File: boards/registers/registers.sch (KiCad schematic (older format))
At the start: 51 parts

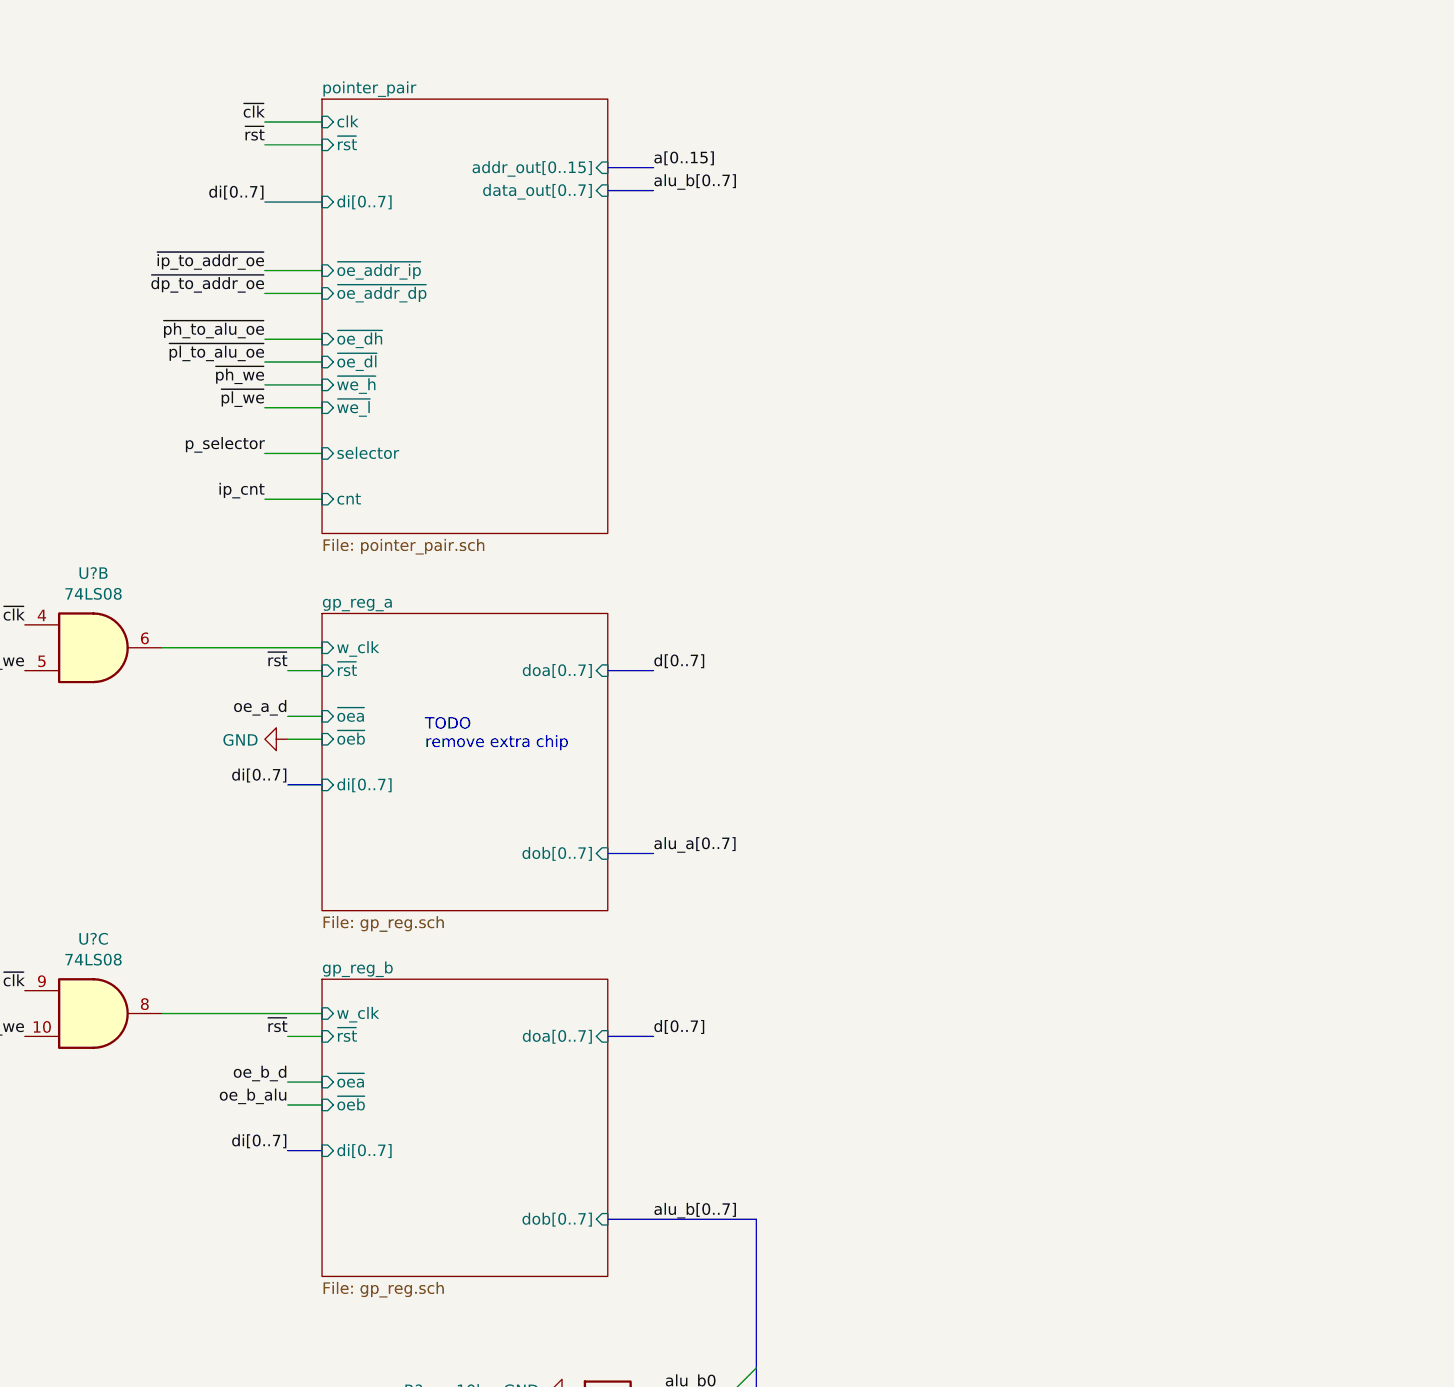
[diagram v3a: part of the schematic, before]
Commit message: Remove redundant chip from the register A, change hierarchical pin types
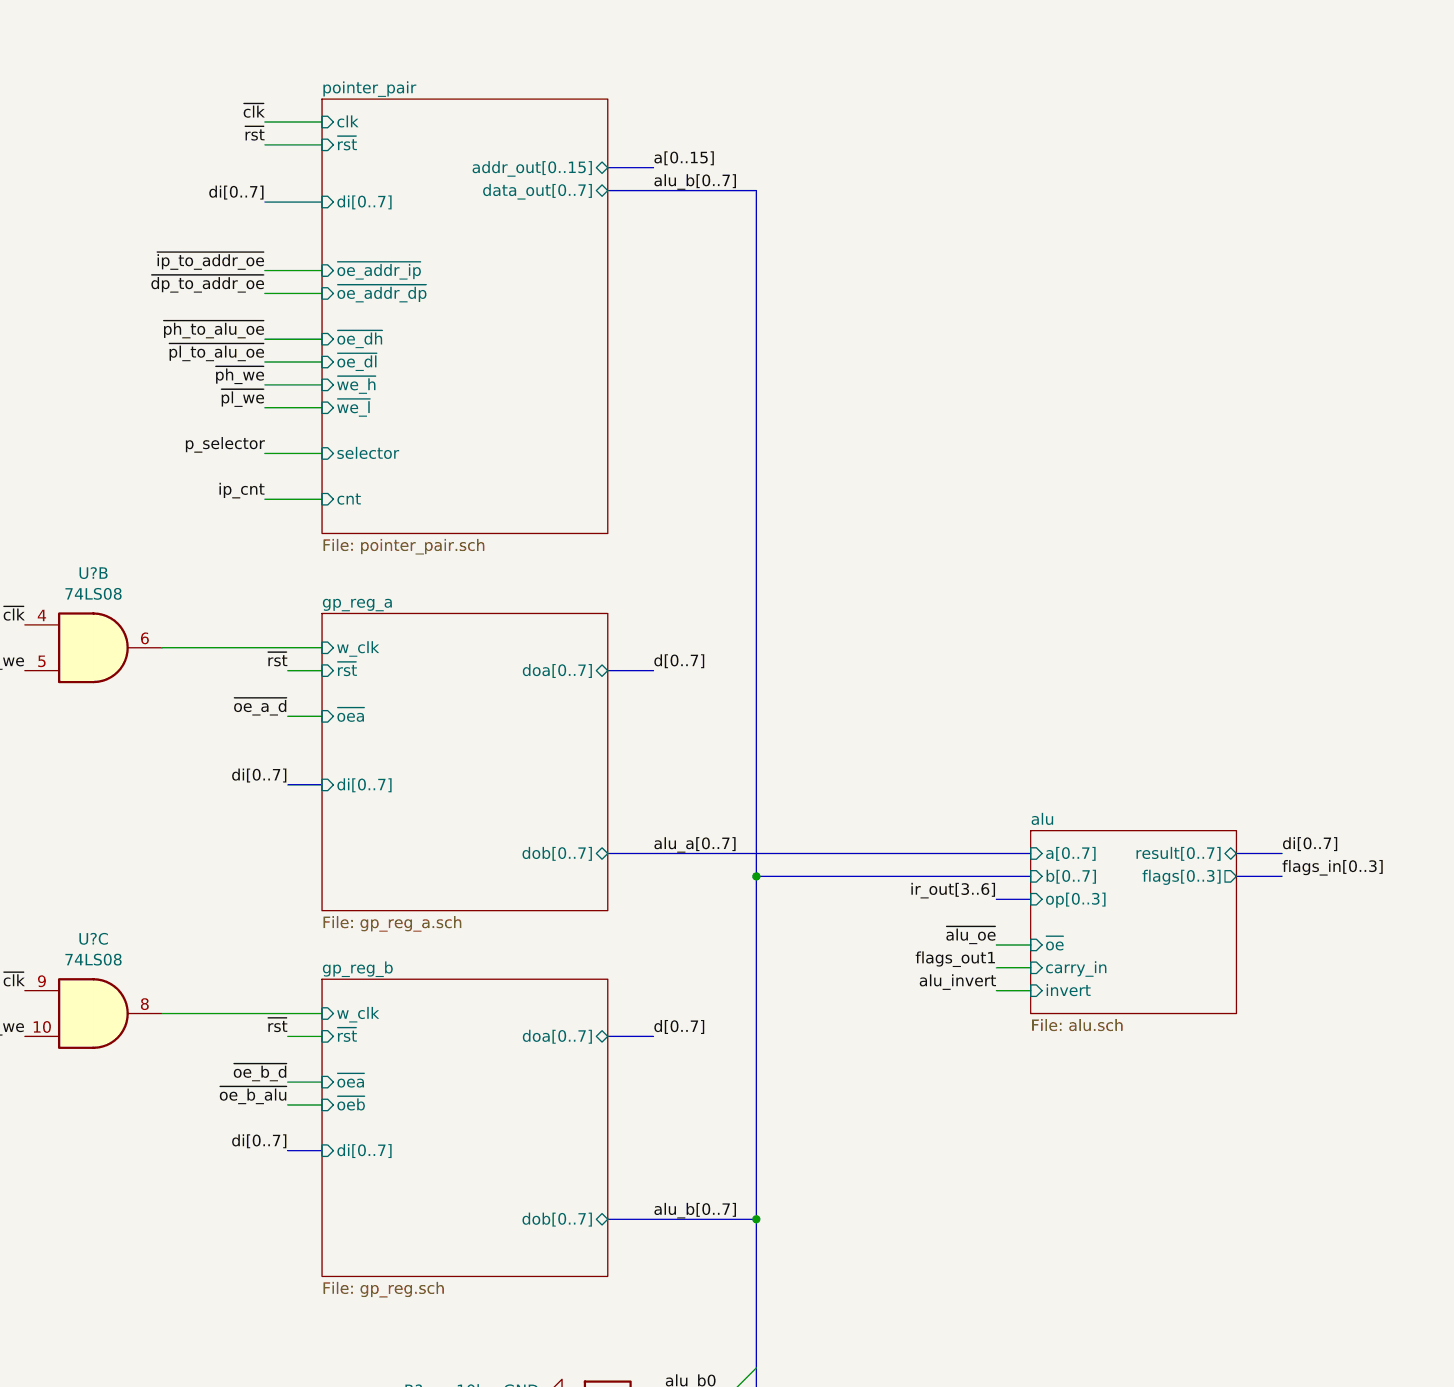
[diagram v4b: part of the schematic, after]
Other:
- note removed: "TODO\nremove extra chip"
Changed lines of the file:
@@
 $Descr A3 16535 11693
 encoding utf-8
-Sheet 1 6
+Sheet 1 7
 Title "CPU registers and memory module"
 Date "2019-12-28"
@@
 F11 "~we_l" I L 10150 2400 50
 F12 "selector" I L 10150 2600 50
-F13 "addr_out[0..15]" I R 11400 1350 50
-F14 "data_out[0..7]" I R 11400 1450 50
+F13 "addr_out[0..15]" T R 11400 1350 50
+F14 "data_out[0..7]" T R 11400 1450 50
 $EndSheet
 Wire Bus Line
@@
 Text Label 9900 1500 2    50   ~ 0
 di[0..7]
-Wire Bus Line
-	11400 1450 11600 1450
 Text Label 11600 1450 0    50   ~ 0
 alu_b[0..7]
@@
 ir_we
 $Sheet
-S 10150 3300 1250 1300
-U 5E73B7F6
-F0 "gp_reg_a" 50
-F1 "gp_reg.sch" 50
-F2 "w_clk" I L 10150 3450 50
-F3 "~rst" I L 10150 3550 50
-F4 "~oea" I L 10150 3750 50
-F5 "~oeb" I L 10150 3850 50
-F6 "di[0..7]" I L 10150 4050 50
-F7 "doa[0..7]" I R 11400 3550 50
-F8 "dob[0..7]" I R 11400 4350 50
-$EndSheet
-$Sheet
 S 10150 4900 1250 1300
 U 5E7CA397
@@
 F5 "~oeb" I L 10150 5450 50
 F6 "di[0..7]" I L 10150 5650 50
-F7 "doa[0..7]" I R 11400 5150 50
-F8 "dob[0..7]" I R 11400 5950 50
+F7 "doa[0..7]" T R 11400 5150 50
+F8 "dob[0..7]" T R 11400 5950 50
 $EndSheet
 $Comp
@@
 Wire Wire Line
 	10150 3750 10000 3750
-Wire Wire Line
-	10150 3850 10000 3850
 Wire Bus Line
 	10150 4050 10000 4050
@@
 di[0..7]
 Text Label 10000 3750 2    50   ~ 0
-oe_a_d
-$Comp
-L power:GND #PWR?
-U 1 1 5E7EB4E9
-P 10000 3850
-F 0 "#PWR?" H 10000 3600 50  0001 C CNN
-F 1 "GND" V 10005 3722 50  0000 R CNN
-F 2 "" H 10000 3850 50  0001 C CNN
-F 3 "" H 10000 3850 50  0001 C CNN
-	1    10000 3850
-	0    1    1    0
-$EndComp
-Text Notes 10600 3900 0    50   ~ 0
-TODO\nremove extra chip
-Wire Bus Line
-	11400 3550 11600 3550
+~oe_a_d
 Text Label 11600 4350 0    50   ~ 0
 alu_a[0..7]
 Text Label 11600 3550 0    50   ~ 0
 d[0..7]
-Wire Bus Line
-	11600 4350 11400 4350
 Wire Bus Line
 	11400 5150 11600 5150
@@
 di[0..7]
 Text Label 10000 5350 2    50   ~ 0
-oe_b_d
+~oe_b_d
 Text Label 10000 5450 2    50   ~ 0
-oe_b_alu
+~oe_b_alu
 Text Label 8850 4950 2    50   ~ 0
 ~clk
@@
 U 1 1 5E9A723F
 P 6000 1100
+AR Path="/5E7CA397/5E9A723F" Ref="R?"  Part="1"
+AR Path="/5E9A723F" Ref="R?"  Part="1"
 F 0 "R?" V 6000 1900 50  0000 C CNN
 F 1 "1k" V 6000 1750 50  0000 C CNN
@@
 U 1 1 5E9A7245
 P 6000 1200
+AR Path="/5E7CA397/5E9A7245" Ref="R?"  Part="1"
+AR Path="/5E9A7245" Ref="R?"  Part="1"
 F 0 "R?" V 6000 2000 50  0000 C CNN
 F 1 "1k" V 6000 1850 50  0000 C CNN
@@
 U 1 1 5E9A724B
 P 6000 1300
+AR Path="/5E7CA397/5E9A724B" Ref="R?"  Part="1"
+AR Path="/5E9A724B" Ref="R?"  Part="1"
 F 0 "R?" V 6000 2100 50  0000 C CNN
 F 1 "1k" V 6000 1950 50  0000 C CNN
@@
 U 1 1 5E9A7251
 P 6000 1400
+AR Path="/5E7CA397/5E9A7251" Ref="R?"  Part="1"
+AR Path="/5E9A7251" Ref="R?"  Part="1"
 F 0 "R?" V 6000 2200 50  0000 C CNN
 F 1 "1k" V 6000 2050 50  0000 C CNN
@@
 U 1 1 5E9A7257
 P 6000 1500
+AR Path="/5E7CA397/5E9A7257" Ref="R?"  Part="1"
+AR Path="/5E9A7257" Ref="R?"  Part="1"
 F 0 "R?" V 6000 2300 50  0000 C CNN
 F 1 "1k" V 6000 2150 50  0000 C CNN
@@
 U 1 1 5E9A725D
 P 6000 1600
+AR Path="/5E7CA397/5E9A725D" Ref="R?"  Part="1"
+AR Path="/5E9A725D" Ref="R?"  Part="1"
 F 0 "R?" V 6000 2400 50  0000 C CNN
 F 1 "1k" V 6000 2250 50  0000 C CNN
@@
 U 1 1 5E9A7263
 P 6000 1700
+AR Path="/5E7CA397/5E9A7263" Ref="R?"  Part="1"
+AR Path="/5E9A7263" Ref="R?"  Part="1"
 F 0 "R?" V 6000 2500 50  0000 C CNN
 F 1 "1k" V 6000 2350 50  0000 C CNN
@@
 U 1 1 5E9A7269
 P 6000 1800
+AR Path="/5E7CA397/5E9A7269" Ref="R?"  Part="1"
+AR Path="/5E9A7269" Ref="R?"  Part="1"
 F 0 "R?" V 6000 2600 50  0000 C CNN
 F 1 "1k" V 6000 2450 50  0000 C CNN
@@
 	0    1    1    0
 $EndComp
+$Sheet
+S 13250 4250 900  800
+U 5E9B4830
+F0 "alu" 50
+F1 "alu.sch" 50
+F2 "a[0..7]" I L 13250 4350 50
+F3 "b[0..7]" I L 13250 4450 50
+F4 "op[0..3]" I L 13250 4550 50
+F5 "~oe" I L 13250 4750 50
+F6 "carry_in" I L 13250 4850 50
+F7 "invert" I L 13250 4950 50
+F8 "result[0..7]" T R 14150 4350 50
+F9 "flags[0..3]" O R 14150 4450 50
+$EndSheet
+Wire Bus Line
+	12050 5950 12050 4450
+Wire Bus Line
+	12050 4450 13250 4450
+Connection ~ 12050 5950
+Wire Bus Line
+	12050 1450 12050 4450
+Wire Bus Line
+	11400 1450 12050 1450
+Connection ~ 12050 4450
+Wire Wire Line
+	13250 4750 13100 4750
+Wire Wire Line
+	13250 4850 13100 4850
+Wire Wire Line
+	13250 4950 13100 4950
+Text Label 13100 4750 2    50   ~ 0
+~alu_oe
+Text Label 13100 4850 2    50   ~ 0
+flags_out1
+Text Label 13100 4950 2    50   ~ 0
+alu_invert
+Wire Bus Line
+	13250 4550 13100 4550
+Text Label 13100 4550 2    50   ~ 0
+ir_out[3..6]
+Wire Bus Line
+	14150 4450 14350 4450
+Text Label 14350 4450 0    50   ~ 0
+flags_in[0..3]
+Wire Bus Line
+	14150 4350 14350 4350
+Text Label 14350 4350 0    50   ~ 0
+di[0..7]
+$Sheet
+S 10150 3300 1250 1300
+U 5E9FD18D
+F0 "gp_reg_a" 50
+F1 "gp_reg_a.sch" 50
+F2 "w_clk" I L 10150 3450 50
+F3 "~rst" I L 10150 3550 50
+F4 "di[0..7]" I L 10150 4050 50
+F5 "doa[0..7]" T R 11400 3550 50
+F6 "dob[0..7]" T R 11400 4350 50
+F7 "~oea" I L 10150 3750 50
+$EndSheet
+Wire Bus Line
+	11600 3550 11400 3550
+Wire Bus Line
+	11400 4350 13250 4350
 Wire Bus Line
 	4350 6100 4350 6750

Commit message: Control unit and ALU interfaces, gp_reg_a
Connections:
- net a_we renamed we_a
- net b_we renamed we_b
- net ir_we renamed we_ir
- net ~d_to_di_oe renamed ~oe_d_di
- net ~flags_we renamed ~we_flags
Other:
- moved on the sheet: C?, D?, R?, U?, U?A, U?B, U?C

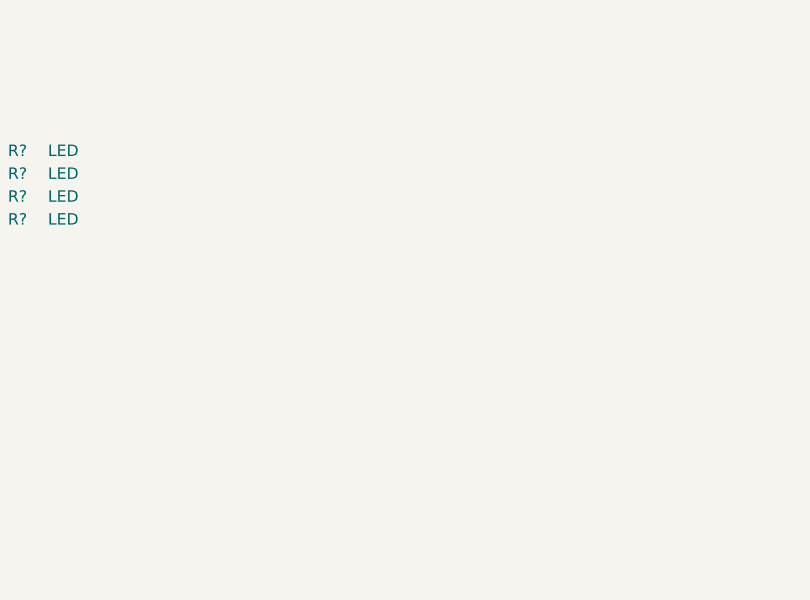
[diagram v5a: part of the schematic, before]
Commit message: Almost complete CPU registers module schematics
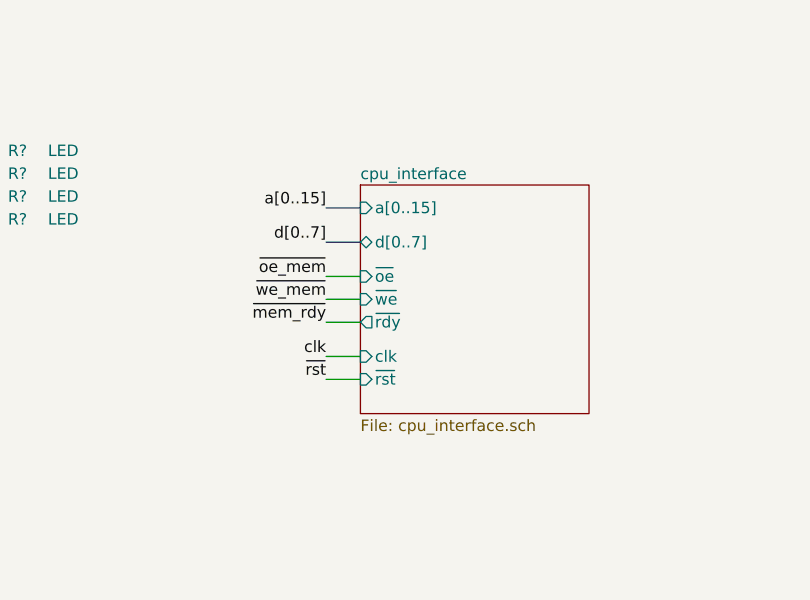
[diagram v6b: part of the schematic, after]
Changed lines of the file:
@@
 $Descr A3 16535 11693
 encoding utf-8
-Sheet 1 8
+Sheet 1 9
 Title "CPU registers and memory module"
 Date "2019-12-28"
@@
 Wire Wire Line
 	11300 1900 11050 1900
-Wire Bus Line
-	2350 6050 2350 6700
-Wire Bus Line
-	4400 6200 4400 7700
-Wire Bus Line
-	4450 850  4450 1650
-Wire Bus Line
-	13200 5950 13200 7650
-Wire Bus Line
-	4400 3450 4400 5900
-Wire Bus Line
-	2400 1150 2400 4750
 Text Label 11050 1900 2    50   ~ 0
 addr_dp
@@
 Text Label 8750 3850 0    50   ~ 0
 p_selector
+$Sheet
+S 7500 7450 1000 1000
+U 5EC337E5
+F0 "cpu_interface" 50
+F1 "cpu_interface.sch" 50
+F2 "a[0..15]" I L 7500 7550 50
+F3 "d[0..7]" B L 7500 7700 50
+F4 "~oe" I L 7500 7850 50
+F5 "~we" I L 7500 7950 50
+F6 "~rdy" O L 7500 8050 50
+F7 "clk" I L 7500 8200 50
+F8 "~rst" I L 7500 8300 50
+$EndSheet
+Wire Bus Line
+	7500 7550 7350 7550
+Wire Bus Line
+	7500 7700 7350 7700
+Text Label 7350 7550 2    50   ~ 0
+a[0..15]
+Text Label 7350 7700 2    50   ~ 0
+d[0..7]
+Wire Wire Line
+	7500 7850 7350 7850
+Wire Wire Line
+	7500 7950 7350 7950
+Wire Wire Line
+	7500 8050 7350 8050
+Wire Wire Line
+	7500 8200 7350 8200
+Wire Wire Line
+	7500 8300 7350 8300
+Wire Bus Line
+	2350 6050 2350 6700
+Wire Bus Line
+	4400 6200 4400 7700
+Wire Bus Line
+	4450 850  4450 1650
+Wire Bus Line
+	13200 5950 13200 7650
+Wire Bus Line
+	4400 3450 4400 5900
+Wire Bus Line
+	2400 1150 2400 4750
+Text Label 7350 8200 2    50   ~ 0
+clk
+Text Label 7350 8300 2    50   ~ 0
+~rst
+Text Label 7350 8050 2    50   ~ 0
+~mem_rdy
+Text Label 7350 7850 2    50   ~ 0
+~oe_mem
+Text Label 7350 7950 2    50   ~ 0
+~we_mem
 $EndSCHEMATC

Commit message: Power and clock circuitry
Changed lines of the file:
@@
 $Descr A3 16535 11693
 encoding utf-8
-Sheet 1 9
+Sheet 1 10
 Title "CPU registers and memory module"
 Date "2019-12-28"
@@
 Wire Wire Line
 	7500 8300 7350 8300
-Wire Bus Line
-	2350 6050 2350 6700
-Wire Bus Line
-	4400 6200 4400 7700
-Wire Bus Line
-	4450 850  4450 1650
-Wire Bus Line
-	13200 5950 13200 7650
-Wire Bus Line
-	4400 3450 4400 5900
-Wire Bus Line
-	2400 1150 2400 4750
 Text Label 7350 8200 2    50   ~ 0
 clk
@@
 Text Label 7350 7950 2    50   ~ 0
 ~we_mem
+$Sheet
+S 7500 950  550  600
+U 5EF05415
+F0 "pwr_and_clk" 50
+F1 "pwr_and_clk.sch" 50
+F2 "clk" O R 8050 1100 50
+F3 "~rst" O R 8050 1450 50
+F4 "~clk" O R 8050 1200 50
+$EndSheet
+Wire Wire Line
+	8050 1100 8150 1100
+Wire Wire Line
+	8150 1200 8050 1200
+Wire Wire Line
+	8150 1450 8050 1450
+Wire Bus Line
+	2350 6050 2350 6700
+Wire Bus Line
+	4400 6200 4400 7700
+Wire Bus Line
+	4450 850  4450 1650
+Wire Bus Line
+	13200 5950 13200 7650
+Wire Bus Line
+	4400 3450 4400 5900
+Wire Bus Line
+	2400 1150 2400 4750
+Text Label 8150 1100 0    50   ~ 0
+clk
+Text Label 8150 1200 0    50   ~ 0
+~clk
+Text Label 8150 1450 0    50   ~ 0
+~rst
 $EndSCHEMATC

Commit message: Fix unconnected nets
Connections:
- net ir_out2 is gone; now on net alu_invert: D?.2 (A), U?.6 (Q2)
- net ir_out3 renamed alu_op0
- net ir_out4 renamed alu_op1
- net ir_out5 renamed alu_op2
- net ir_out6 renamed alu_op3
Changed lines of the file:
@@
 U 1 1 5E6ECBBA
 P 3350 4150
-F 0 "U?" H 3700 3600 50  0000 C CNN
+F 0 "U?" H 3750 3600 50  0000 C CNN
 F 1 "74AC273" H 3800 3500 50  0000 C CNN
 F 2 "" H 3350 4150 50  0001 C CNN
@@
 U 1 1 5E6F3C0E
 P 3350 1550
-F 0 "U?" H 3700 1000 50  0000 C CNN
+F 0 "U?" H 3750 1000 50  0000 C CNN
 F 1 "74ACT244" H 3650 900 50  0000 C CNN
 F 2 "" H 3350 1550 50  0001 C CNN
@@
 U 1 1 5E857F06
 P 3350 6800
-F 0 "U?" H 3700 6250 50  0000 C CNN
+F 0 "U?" H 3750 6250 50  0000 C CNN
 F 1 "74LS161" H 3650 6150 50  0000 C CNN
 F 2 "" H 3350 6800 50  0001 C CNN
@@
 Text Label 14250 4950 2    50   ~ 0
 alu_invert
-Wire Bus Line
-	14400 4550 14250 4550
-Text Label 14250 4550 2    50   ~ 0
-ir_out[3..6]
 Wire Bus Line
 	15300 4450 15500 4450
@@
 ~mem_rdy
 Text Label 7350 7850 2    50   ~ 0
-~oe_mem
+~oe
 Text Label 7350 7950 2    50   ~ 0
-~we_mem
+~we
 $Sheet
 S 7500 950  550  600
@@
 Wire Wire Line
 	8150 1450 8050 1450
-Wire Bus Line
-	2350 6050 2350 6700
-Wire Bus Line
-	4400 6200 4400 7700
-Wire Bus Line
-	4450 850  4450 1650
-Wire Bus Line
-	13200 5950 13200 7650
-Wire Bus Line
-	4400 3450 4400 5900
-Wire Bus Line
-	2400 1150 2400 4750
 Text Label 8150 1100 0    50   ~ 0
 clk
@@
 Text Label 8150 1450 0    50   ~ 0
 ~rst
+Wire Bus Line
+	14400 4550 13750 4550
+Text Label 13750 5100 1    50   ~ 0
+alu_op[0..3]
+Entry Wire Line
+	13750 5650 13850 5550
+Entry Wire Line
+	13750 5750 13850 5650
+Entry Wire Line
+	13750 5850 13850 5750
+Entry Wire Line
+	13750 5950 13850 5850
+Text Label 13850 5550 0    50   ~ 0
+alu_op0
+Text Label 13850 5650 0    50   ~ 0
+alu_op1
+Text Label 13850 5750 0    50   ~ 0
+alu_op2
+Text Label 13850 5850 0    50   ~ 0
+alu_op3
+Text Label 14300 5550 0    50   ~ 0
+ir_out3
+Text Label 14300 5650 0    50   ~ 0
+ir_out4
+Text Label 14300 5750 0    50   ~ 0
+ir_out5
+Text Label 14300 5850 0    50   ~ 0
+ir_out6
+Wire Wire Line
+	13850 5550 14300 5550
+Wire Wire Line
+	13850 5650 14300 5650
+Wire Wire Line
+	13850 5750 14300 5750
+Wire Wire Line
+	13850 5850 14300 5850
+Text Label 14300 5450 0    50   ~ 0
+ir_out2
+Wire Wire Line
+	14300 5450 14250 5450
+Wire Wire Line
+	14250 5450 14250 4950
+Wire Bus Line
+	2350 6050 2350 6700
+Wire Bus Line
+	13750 4550 13750 5950
+Wire Bus Line
+	4400 6200 4400 7700
+Wire Bus Line
+	4450 850  4450 1650
+Wire Bus Line
+	13200 5950 13200 7650
+Wire Bus Line
+	4400 3450 4400 5900
+Wire Bus Line
+	2400 1150 2400 4750
 $EndSCHEMATC
